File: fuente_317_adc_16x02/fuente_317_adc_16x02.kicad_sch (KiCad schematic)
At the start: 78 parts, among them J1 Fuente, J10 3V3, J11 GND, J12 +12V, J13 -12V, J14 +1.2V, J15 -1.2V, J16 -5V, J17 Vadj+, J18 Vadj-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

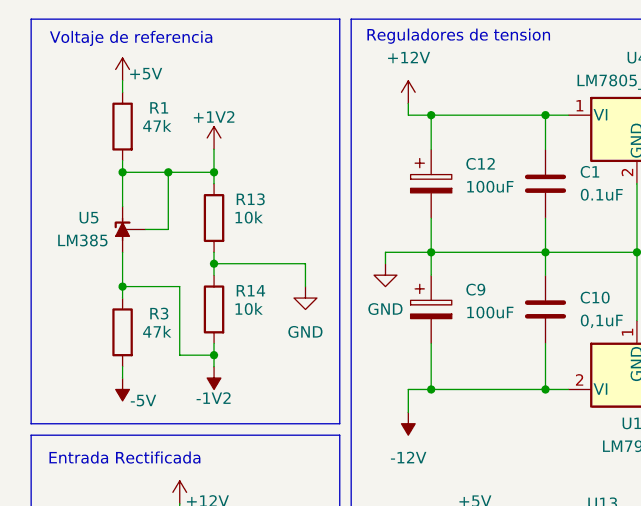
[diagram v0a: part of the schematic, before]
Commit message: fuente_317_337: start to wire OP AMP
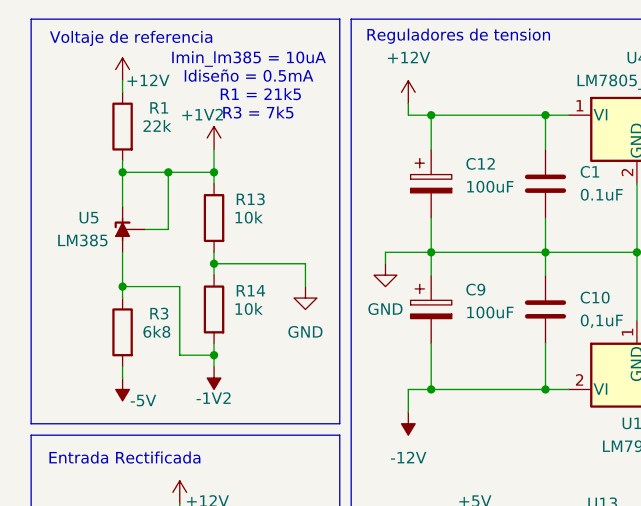
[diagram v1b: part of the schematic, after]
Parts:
- R1: value 47k -> 22k
- R3: value 47k -> 6k8
- R30, R31, R32, R33, R34, R35, R37, R38, R39, R8, R9: footprint Resistor_THT:R_Axial_DIN0207_L6.3mm_D2.5mm_P10.16mm_Horizontal -> Resistor_THT:R_Axial_DIN0207_L6.3mm_D2.5mm_P5.08mm_Vertical
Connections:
- net +12V: now also R1.1
- net +5V: no longer R1.1
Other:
- note added: "Imin_lm385 = 10uA Idiseño = 0.5mA R1 = 21k5 R3 = 7k5"
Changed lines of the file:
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@@
 		)
 	)
+	(text "Imin_lm385 = 10uA\nIdiseño = 0.5mA\n	 R1 = 21k5\n	R3 = 7k5\n"
+		(exclude_from_sim no)
+		(at 38.1 21.082 0)
+		(effects
+			(font
+				(size 1.27 1.27)
+			)
+		)
+	)
 	(text "ESP8266"
 		(exclude_from_sim no)
@@
 			)
 		)
-		(property "Footprint" "Resistor_THT:R_Axial_DIN0207_L6.3mm_D2.5mm_P10.16mm_Horizontal"
+		(property "Footprint" "Resistor_THT:R_Axial_DIN0207_L6.3mm_D2.5mm_P5.08mm_Vertical"
 			(at 247.65 27.432 90)
 			(effects
@@
 	)
 	(symbol
-		(lib_id "power:+5V")
-		(at 24.13 20.32 0)
-		(unit 1)
-		(exclude_from_sim no)
-		(in_bom yes)
-		(on_board yes)
-		(dnp no)
-		(property "Reference" "#PWR015"
-			(at 24.13 24.13 0)
-			(effects
-				(font
-					(size 1.27 1.27)
-				)
-				(hide yes)
-			)
-		)
-		(property "Value" "+5V"
-			(at 26.67 19.558 0)
-			(effects
-				(font
-					(size 1.27 1.27)
-				)
-			)
-		)
-		(property "Footprint" ""
-			(at 24.13 20.32 0)
-			(effects
-				(font
-					(size 1.27 1.27)
-				)
-				(hide yes)
-			)
-		)
-		(property "Datasheet" ""
-			(at 24.13 20.32 0)
-			(effects
-				(font
-					(size 1.27 1.27)
-				)
-				(hide yes)
-			)
-		)
-		(property "Description" "Power symbol creates a global label with name \"+5V\""
-			(at 24.13 20.32 0)
-			(effects
-				(font
-					(size 1.27 1.27)
-				)
-				(hide yes)
-			)
-		)
-		(pin "1"
-		)
-		(instances
-			(project "fuente_317_adc"
-				(path "/582826ff-9970-4283-a88f-29ce31fb61c2"
-					(reference "#PWR015")
-					(unit 1)
-				)
-			)
-		)
-	)
-	(symbol
 		(lib_id "Connector:Conn_01x02_Pin")
 		(at 265.43 146.05 0)
@@
 			)
 		)
-		(property "Footprint" "Resistor_THT:R_Axial_DIN0207_L6.3mm_D2.5mm_P10.16mm_Horizontal"
+		(property "Footprint" "Resistor_THT:R_Axial_DIN0207_L6.3mm_D2.5mm_P5.08mm_Vertical"
 			(at 234.95 43.942 90)
 			(effects
@@
 			)
 		)
-		(property "Footprint" "Resistor_THT:R_Axial_DIN0207_L6.3mm_D2.5mm_P10.16mm_Horizontal"
+		(property "Footprint" "Resistor_THT:R_Axial_DIN0207_L6.3mm_D2.5mm_P5.08mm_Vertical"
 			(at 236.22 65.532 90)
 			(effects
@@
 	)
 	(symbol
+		(lib_id "power:+12V")
+		(at 24.13 20.32 0)
+		(unit 1)
+		(exclude_from_sim no)
+		(in_bom yes)
+		(on_board yes)
+		(dnp no)
+		(property "Reference" "#PWR03"
+			(at 24.13 24.13 0)
+			(effects
+				(font
+					(size 1.27 1.27)
+				)
+				(hide yes)
+			)
+		)
+		(property "Value" "+12V"
+			(at 26.924 20.32 0)
+			(effects
+				(font
+					(size 1.27 1.27)
+				)
+			)
+		)
+		(property "Footprint" ""
+			(at 24.13 20.32 0)
+			(effects
+				(font
+					(size 1.27 1.27)
+				)
+				(hide yes)
+			)
+		)
+		(property "Datasheet" ""
+			(at 24.13 20.32 0)
+			(effects
+				(font
+					(size 1.27 1.27)
+				)
+				(hide yes)
+			)
+		)
+		(property "Description" "Power symbol creates a global label with name \"+12V\""
+			(at 24.13 20.32 0)
+			(effects
+				(font
+					(size 1.27 1.27)
+				)
+				(hide yes)
+			)
+		)
+		(pin "1"
+		)
+		(instances
+			(project "fuente_317_adc_16x02"
+				(path "/582826ff-9970-4283-a88f-29ce31fb61c2"
+					(reference "#PWR03")
+					(unit 1)
+				)
+			)
+		)
+	)
+	(symbol
 		(lib_id "Device:R")
 		(at 34.29 35.56 0)
@@
 			)
 		)
-		(property "Footprint" "Resistor_THT:R_Axial_DIN0207_L6.3mm_D2.5mm_P10.16mm_Horizontal"
+		(property "Footprint" "Resistor_THT:R_Axial_DIN0207_L6.3mm_D2.5mm_P5.08mm_Vertical"
 			(at 240.792 82.55 90)
 			(effects
@@
 			)
 		)
-		(property "Footprint" "Resistor_THT:R_Axial_DIN0207_L6.3mm_D2.5mm_P10.16mm_Horizontal"
+		(property "Footprint" "Resistor_THT:R_Axial_DIN0207_L6.3mm_D2.5mm_P5.08mm_Vertical"
 			(at 236.22 115.062 90)
 			(effects
@@
 			)
 		)
-		(property "Footprint" "Resistor_THT:R_Axial_DIN0207_L6.3mm_D2.5mm_P10.16mm_Horizontal"
+		(property "Footprint" "Resistor_THT:R_Axial_DIN0207_L6.3mm_D2.5mm_P5.08mm_Vertical"
 			(at 239.522 50.8 90)
 			(effects
@@
 			)
 		)
-		(property "Footprint" "Resistor_THT:R_Axial_DIN0207_L6.3mm_D2.5mm_P10.16mm_Horizontal"
+		(property "Footprint" "Resistor_THT:R_Axial_DIN0207_L6.3mm_D2.5mm_P5.08mm_Vertical"
 			(at 236.22 75.692 90)
 			(effects
@@
 		)
 		(property "Value" "+1V2"
-			(at 34.29 24.384 0)
+			(at 33.02 24.13 0)
 			(effects
 				(font
@@
 			)
 		)
-		(property "Footprint" "Resistor_THT:R_Axial_DIN0207_L6.3mm_D2.5mm_P10.16mm_Horizontal"
+		(property "Footprint" "Resistor_THT:R_Axial_DIN0207_L6.3mm_D2.5mm_P5.08mm_Vertical"
 			(at 256.54 65.532 90)
 			(effects
@@
 			)
 		)
-		(property "Footprint" "Resistor_THT:R_Axial_DIN0207_L6.3mm_D2.5mm_P10.16mm_Horizontal"
+		(property "Footprint" "Resistor_THT:R_Axial_DIN0207_L6.3mm_D2.5mm_P5.08mm_Vertical"
 			(at 261.62 18.542 90)
 			(effects
@@
 			)
 		)
-		(property "Value" "47k"
+		(property "Value" "6k8"
 			(at 27.94 48.26 0)
 			(effects
@@
 			)
 		)
-		(property "Value" "47k"
+		(property "Value" "22k"
 			(at 27.94 25.4 0)
 			(effects
@@
 			)
 		)
-		(property "Footprint" "Resistor_THT:R_Axial_DIN0207_L6.3mm_D2.5mm_P10.16mm_Horizontal"
+		(property "Footprint" "Resistor_THT:R_Axial_DIN0207_L6.3mm_D2.5mm_P5.08mm_Vertical"
 			(at 239.522 100.33 90)
 			(effects
@@
 			)
 		)
-		(property "Footprint" "Resistor_THT:R_Axial_DIN0207_L6.3mm_D2.5mm_P10.16mm_Horizontal"
+		(property "Footprint" "Resistor_THT:R_Axial_DIN0207_L6.3mm_D2.5mm_P5.08mm_Vertical"
 			(at 256.54 115.062 90)
 			(effects

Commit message: Change position of LM7805 and 3v3
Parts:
- R31, R8: footprint Resistor_THT:R_Axial_DIN0207_L6.3mm_D2.5mm_P5.08mm_Vertical -> Resistor_THT:R_Axial_DIN0207_L6.3mm_D2.5mm_P10.16mm_Horizontal
- R33, R38: value 47k -> 10k
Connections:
- net GND: now also U6.6 (-); no longer U6.3 (+)
- net Iadc-: now also U6.1; no longer U6.7
- net Vadc-: now also U6.7; no longer U6.1
- net at R8.2, R9.1: now also U6.5 (+); no longer U6.2 (-)
- net at R32.2, R33.1: now also U6.2 (-); no longer U6.5 (+)
- net at R34.2, R35.1: now also U6.3 (+); no longer U6.6 (-)
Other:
- moved on the sheet: U6A, U6B
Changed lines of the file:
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@@
 			)
 		)
-		(property "Footprint" "Resistor_THT:R_Axial_DIN0207_L6.3mm_D2.5mm_P5.08mm_Vertical"
+		(property "Footprint" "Resistor_THT:R_Axial_DIN0207_L6.3mm_D2.5mm_P10.16mm_Horizontal"
 			(at 247.65 27.432 90)
 			(effects
@@
 	(symbol
 		(lib_id "Amplifier_Operational:LM324")
-		(at 261.62 31.75 0)
+		(at 256.54 57.15 0)
 		(mirror x)
 		(unit 1)
@@
 		(dnp no)
 		(property "Reference" "U6"
-			(at 261.366 26.924 0)
+			(at 256.286 52.324 0)
 			(effects
 				(font
@@
 		)
 		(property "Value" "LM324"
-			(at 261.366 24.384 0)
+			(at 256.286 49.784 0)
 			(effects
 				(font
@@
 		)
 		(property "Footprint" "Package_DIP:CERDIP-14_W7.62mm_SideBrazed_Socket"
-			(at 260.35 34.29 0)
+			(at 255.27 59.69 0)
 			(effects
 				(font
@@
 		)
 		(property "Datasheet" "http://www.ti.com/lit/ds/symlink/lm2902-n.pdf"
-			(at 262.89 36.83 0)
+			(at 257.81 62.23 0)
 			(effects
 				(font
@@
 		)
 		(property "Description" "Low-Power, Quad-Operational Amplifiers, DIP-14/SOIC-14/SSOP-14"
-			(at 261.62 31.75 0)
+			(at 256.54 57.15 0)
 			(effects
 				(font
@@
 	(symbol
 		(lib_id "Amplifier_Operational:LM324")
-		(at 256.54 57.15 0)
+		(at 261.62 31.75 0)
 		(unit 2)
 		(exclude_from_sim no)
@@
 		(fields_autoplaced yes)
 		(property "Reference" "U6"
-			(at 256.54 46.99 0)
+			(at 261.62 21.59 0)
 			(effects
 				(font
@@
 		)
 		(property "Value" "LM324"
-			(at 256.54 49.53 0)
+			(at 261.62 24.13 0)
 			(effects
 				(font
@@
 		)
 		(property "Footprint" "Package_DIP:CERDIP-14_W7.62mm_SideBrazed_Socket"
-			(at 255.27 54.61 0)
+			(at 260.35 29.21 0)
 			(effects
 				(font
@@
 		)
 		(property "Datasheet" "http://www.ti.com/lit/ds/symlink/lm2902-n.pdf"
-			(at 257.81 52.07 0)
+			(at 262.89 26.67 0)
 			(effects
 				(font
@@
 		)
 		(property "Description" "Low-Power, Quad-Operational Amplifiers, DIP-14/SOIC-14/SSOP-14"
-			(at 256.54 57.15 0)
+			(at 261.62 31.75 0)
 			(effects
 				(font
@@
 			)
 		)
-		(property "Value" "47k"
+		(property "Value" "10k"
 			(at 237.49 50.8 0)
 			(effects
@@
 			)
 		)
-		(property "Footprint" "Resistor_THT:R_Axial_DIN0207_L6.3mm_D2.5mm_P5.08mm_Vertical"
+		(property "Footprint" "Resistor_THT:R_Axial_DIN0207_L6.3mm_D2.5mm_P10.16mm_Horizontal"
 			(at 236.22 75.692 90)
 			(effects
@@
 			)
 		)
-		(property "Value" "47k"
+		(property "Value" "10k"
 			(at 237.49 100.33 0)
 			(effects
